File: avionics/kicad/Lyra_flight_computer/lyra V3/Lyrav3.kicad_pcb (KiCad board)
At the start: 4 copper layers, 25 x 60 mm, 84 parts, among them J1 Screw_Terminal_01x08, J2 Screw_Terminal_01x06, J3 Conn_01x02, J4 Conn_01x02, J5 Conn_01x03, J6 Conn_01x06, J7 USB_B_Micro, J8 Conn_01x04, Q1 AO3401A, Q2 AO3400A, Q3 AO3400A, Q4 AO3400A, Q5 AO3400A, U1 AZ1117-3.3, U2 BMI088, U3 MPL3115A2, U4 ADXL375BCCZ-RL7, U5 LIS3MDL, U6 ADS1015IDGS, U7 W25Q64JVXGIQ, U8 RP2040, X1 S3D12.288000B20F30T

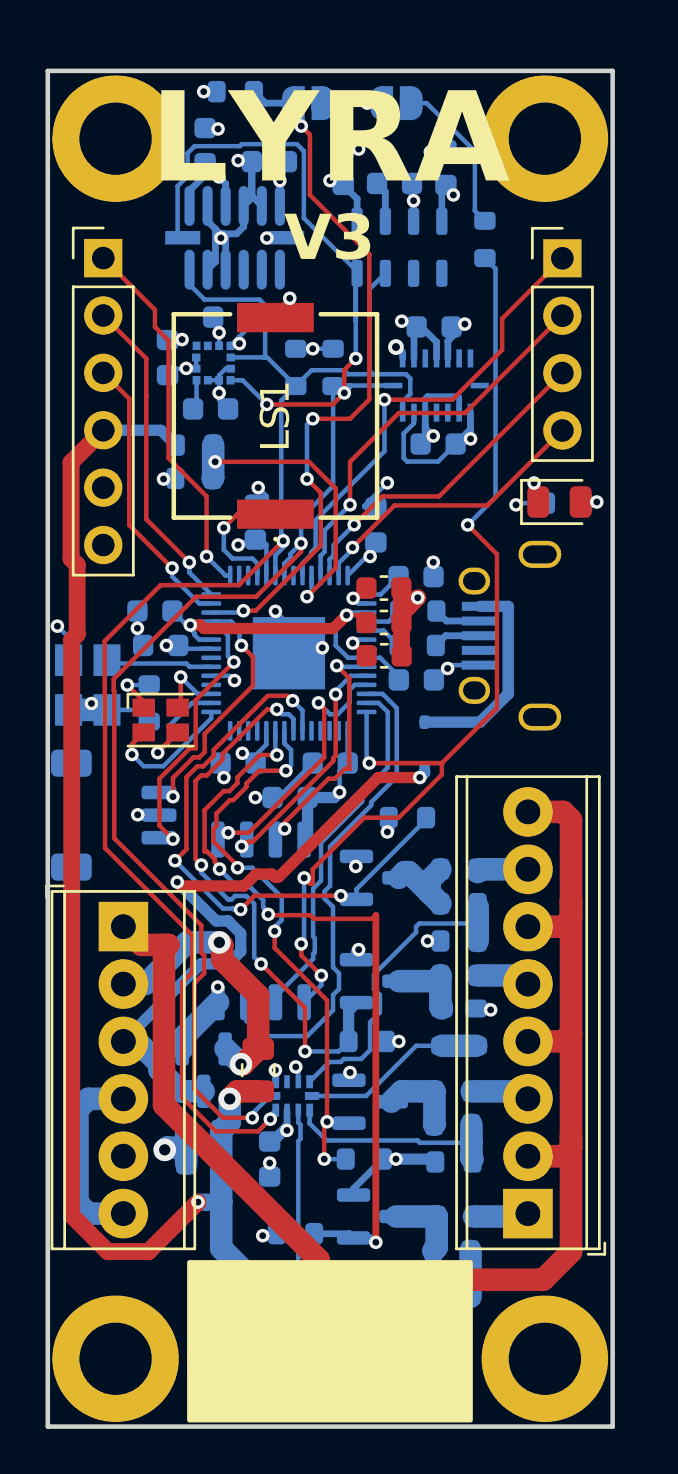
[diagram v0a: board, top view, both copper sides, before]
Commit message: silkscreen work and add parser to display rotation data
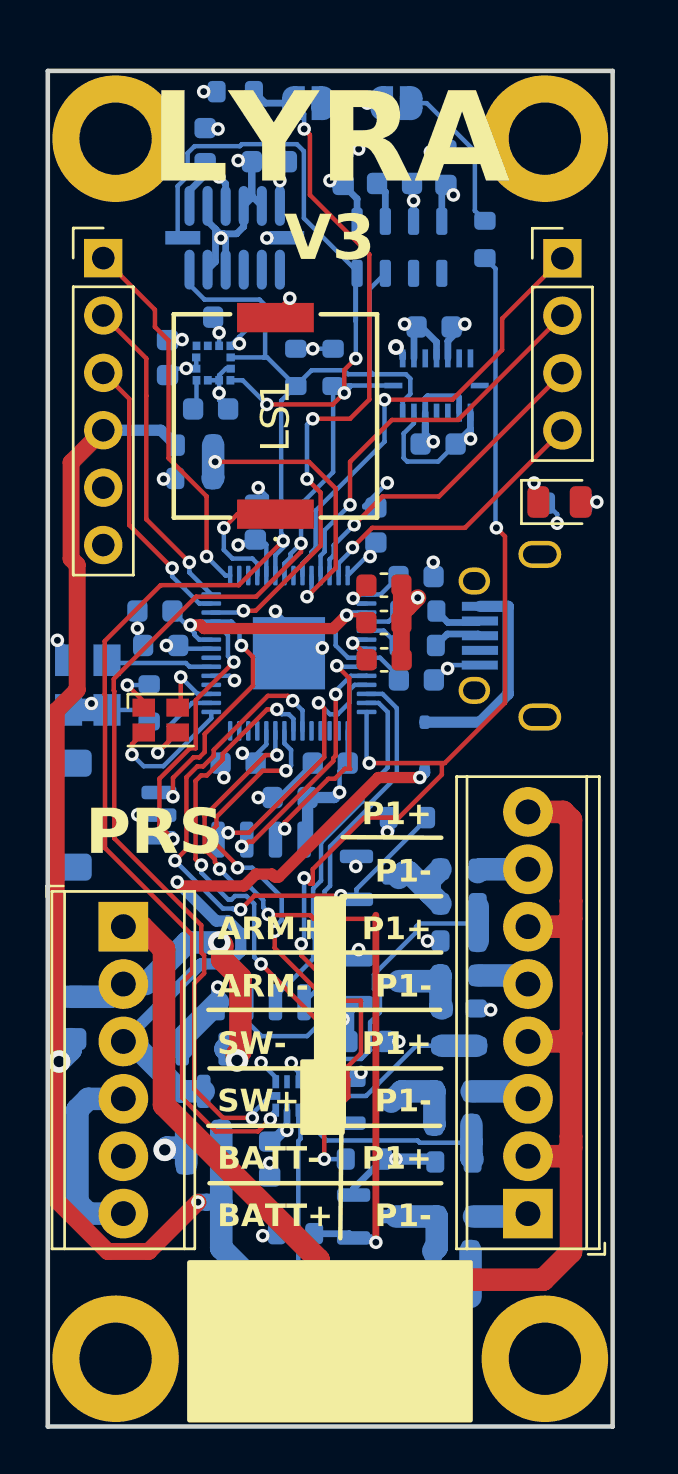
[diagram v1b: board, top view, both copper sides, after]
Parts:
- F1: moved to B.Cu
- moved F1 8.62 mm to (184.6, 100.9)
- moved C20 0.18 mm to (198.5, 85.1)
- moved C19 0.13 mm to (198.5, 81.8)
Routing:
- net /P3 EN : track 26.0 -> 28.0 mm
- net +12P: track 11.5 -> 13.0 mm
- net +12VA: track 67.3 -> 66.1 mm
- net /P2 EN : track 25.2 -> 24.2 mm
- net /QSPI_SS: track 45.5 -> 44.8 mm
- net +3V3: track 57.8 -> 58.4 mm
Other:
- board text added: "ARM+"
- board text added: "ARM-"
- board text added: "BATT+"
- board text added: "BATT-"
- board text added: "JLCJLCJLCJLC"
- board text added: "P1+"
- board text added: "P1-"
- board text added: "PRS"
- board text added: "SW+"
- board text added: "SW-"

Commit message: more lyrav3 work
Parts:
- removed J1: Screw_Terminal_01x08, TerminalBlock_Phoenix:TerminalBlock_Phoenix_MPT-0,5-8-2.54_1x08_P2.54mm_Horizontal
- added J9: Screw_Terminal_01x06, TerminalBlock_Phoenix:TerminalBlock_Phoenix_MPT-0,5-6-2.54_1x06_P2.54mm_Horizontal, F.Cu at (205.0, 110.7)
- J5: footprint Connector_JST:JST_SH_SM03B-SRSS-TB_1x03-1MP_P1.00mm_Horizontal -> Connector_PinHeader_2.00mm:PinHeader_1x03_P2.00mm_Vertical
- moved F1 10.2 mm to (192.8, 107.1)
- moved C3 5.40 mm to (196.2, 68.7)
- moved C4 5.40 mm to (200.8, 68.7)
- moved C1 5.40 mm to (200.4, 80.9)
- moved C10 5.40 mm to (193.0, 68.4)
- moved C12 5.40 mm to (188.5, 77.1)
- moved C13 5.40 mm to (191.3, 75.3)
- moved C14 5.40 mm to (190.4, 79.4)
- moved C2 5.40 mm to (200.3, 75.7)
- moved C9 5.40 mm to (198.5, 69.4)
- moved R4 5.40 mm to (189.7, 81.0)
- moved R5 5.40 mm to (189.6, 82.4)
- moved R6 5.40 mm to (195.8, 77.5)
- moved R7 5.40 mm to (194.1, 77.5)
- moved U2 5.40 mm to (200.4, 78.3)
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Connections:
- J2 pad 1: /PYRO PWR -> /P4-
- J2 pad 2: +12P -> /PYRO PWR
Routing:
- net /I2C1 SCL: track 77.1 -> 0.00 mm, vias 5 -> 0
- net GND: track 76.6 -> 0.00 mm, vias 44 -> 0
- net /I2C1 SDA: track 68.2 -> 0.00 mm, vias 2 -> 0
- net +12VA: track 66.1 -> 0.00 mm, vias 2 -> 0
- net /PYRO PWR: track 62.2 -> 0.00 mm
- net +3V3: track 58.4 -> 0.00 mm, vias 24 -> 0
- net /QSPI_SS: track 44.8 -> 0.00 mm, vias 5 -> 0
- net /P4 EN : track 33.6 -> 0.00 mm, vias 4 -> 0
- net /RUN: track 31.4 -> 0.00 mm, vias 4 -> 0
- net +12V: track 29.4 -> 0.00 mm, vias 2 -> 0
- net /P3 EN : track 28.0 -> 0.00 mm, vias 5 -> 0
- net /P1 EN : track 25.2 -> 0.00 mm, vias 4 -> 0
- net /P2 EN : track 24.2 -> 0.00 mm, vias 4 -> 0
- net /QSPI_SD2: track 22.3 -> 0.00 mm
- net /BRKOUT1: track 20.6 -> 0.00 mm, vias 1 -> 0
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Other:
- board size 25 x 60 mm -> 25 x 55 mm

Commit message: move aruond
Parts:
- moved R16 17.9 mm to (197.4, 109.8), turned to -90 degrees
- moved R10 16.6 mm to (200.7, 112.4), turned to 180 degrees
- moved R12 16.0 mm to (200.9, 113.9), turned to 0 degrees
- moved R8 14.7 mm to (202.8, 109.0), turned to -90 degrees
- moved Q3 14.5 mm to (200.1, 109.9)
- moved R13 13.4 mm to (204.2, 94.2), turned to -90 degrees
- moved R20 12.7 mm to (195.3, 98.7), turned to -90 degrees
- moved R27 12.1 mm to (200.7, 100.1), turned to 90 degrees
- moved R11 11.5 mm to (202.7, 94.2), turned to 90 degrees
- moved R23 11.3 mm to (195.3, 101.7), turned to -90 degrees
- moved R17 10.7 mm to (197.1, 96.5), turned to -90 degrees
- moved R25 10.1 mm to (195.3, 104.8), turned to -90 degrees
- moved Q5 9.78 mm to (198.0, 99.9), turned to 180 degrees
- moved Q4 8.34 mm to (199.8, 96.4)
- moved R9 7.05 mm to (202.6, 97.2), turned to 90 degrees
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- renumbered J5 to Je
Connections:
- J9 pad 1: /P3- -> /PYRO PWR
- J9 pad 2: /PYRO PWR -> /P1-
- J9 pad 3: /P2- -> /PYRO PWR
- J9 pad 4: /PYRO PWR -> /P2-
- J9 pad 5: /P1- -> /PYRO PWR
- J9 pad 6: /PYRO PWR -> /P3-
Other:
- board text added: "P2+"
- board text added: "P2-"
- board text added: "P3+"
- board text added: "P3-"
- board text added: "P4+"
- board text added: "P4-"
- board text added: "SWD"
- board text removed: "ARM+"
- board text removed: "ARM-"

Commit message: routing twioce
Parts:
- moved D3 6.28 mm to (206.2, 93.2), turned to 90 degrees
- moved C15 4.31 mm to (199.1, 106.6)
- moved F1 3.75 mm to (190.1, 109.7), turned to 0 degrees
- moved C7 3.45 mm to (193.4, 111.0), turned to 0 degrees
- moved C8 2.81 mm to (192.7, 108.7), turned to 90 degrees
- moved C22 1.63 mm to (197.6, 92.5), turned to 0 degrees
- moved LS1 1.11 mm to (193.4, 78.2)
- moved R24 1.01 mm to (201.3, 106.6), turned to -90 degrees
- moved C21 0.85 mm to (197.1, 82.0)
- moved R5 0.81 mm to (190.3, 82.0)
- moved R4 0.81 mm to (190.3, 80.5)
- moved C13 0.80 mm to (191.9, 74.9)
- moved U5 0.80 mm to (191.2, 76.9)
- moved C12 0.80 mm to (189.1, 76.7)
- moved C23 0.78 mm to (192.4, 93.3), turned to -90 degrees
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- renumbered Je to J5
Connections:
- J2 pad 2: /PYRO PWR -> +12P
- J9 pad 1: /PYRO PWR -> +12P
- J9 pad 3: /PYRO PWR -> +12P
- J9 pad 5: /PYRO PWR -> +12P
- U6 pad 4: /P1 CONT  -> /P2 CONT 
- U6 pad 5: /P2 CONT  -> /P1 CONT 
- U6 pad 6: /P3 CONT  -> /P4 CONT 
- U6 pad 7: /P4 CONT  -> /P3 CONT 
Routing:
- net GND: track 0.00 -> 80.0 mm, vias 0 -> 33
- net +12VA: track 0.00 -> 60.9 mm, vias 0 -> 2
- net +12P: track 0.00 -> 56.7 mm, vias 0 -> 2
- net +3V3: track 0.00 -> 54.0 mm, vias 0 -> 20
- net /QSPI_SS: track 0.00 -> 51.0 mm, vias 0 -> 3
- net +12V: track 0.00 -> 46.6 mm, vias 0 -> 1
- net /RUN: track 0.00 -> 24.6 mm, vias 0 -> 2
- net +1V1: track 0.00 -> 21.8 mm, vias 0 -> 3
- net /QSPI_SD2: track 0.00 -> 20.5 mm, vias 0 -> 2
- net /P3 CONT : track 0.00 -> 19.8 mm, vias 0 -> 2
- net /QSPI_SD1: track 0.00 -> 19.5 mm, vias 0 -> 2
- net /BRKOUT1: track 0.00 -> 18.9 mm, vias 0 -> 1
- net /BRKOUT3: track 0.00 -> 18.4 mm, vias 0 -> 1
- net /QSPI_SDO: track 0.00 -> 18.1 mm, vias 0 -> 2
- net /BRKOUT2: track 0.00 -> 17.2 mm, vias 0 -> 1
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
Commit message: rout lyrav3 fully
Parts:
- moved C26 0.26 mm to (192.8, 81.9)
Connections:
- U8 pad 6: /P1 EN  -> /P4 EN 
- U8 pad 7: /P2 EN  -> /P3 EN 
- U8 pad 8: /P3 EN  -> /P2 EN 
- U8 pad 9: /P4 EN  -> /P1 EN 
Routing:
- net /I2C1 SCL: track 0.00 -> 70.3 mm, vias 0 -> 6
- net /I2C1 SDA: track 0.00 -> 62.1 mm, vias 0 -> 4
- net /P1 EN : track 1.87 -> 31.5 mm, vias 0 -> 2
- net /P2 EN : track 1.88 -> 18.1 mm, vias 0 -> 2
- net /P4 EN : track 1.83 -> 14.0 mm
- net /P3 EN : track 1.81 -> 9.78 mm
- net GND: track 80.0 -> 84.1 mm, vias 33 -> 35
- net +3V3: track 54.0 -> 56.8 mm, vias 20 -> 25
- net /RUN: track 24.6 -> 26.8 mm, vias 2 -> 4
- net /QSPI_SS: track 51.0 -> 52.2 mm
- net +1V1: track 21.8 -> 22.6 mm
- net /QSPI_SD3: track 12.3 -> 11.7 mm
- net Net-(D3-A): track 10.1 -> 9.45 mm
- net /BUZZER: track 1.23 -> 1.82 mm
